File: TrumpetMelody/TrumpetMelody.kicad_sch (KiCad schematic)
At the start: 59 parts, among them J1 USB_B_Micro, J2 Conn_01x05, SW1 SW_Push, SW2 SW_SPST, SW3 SW_SPST, SW4 SW_SPST, U1 STM32F411RETx, U2 TLV62565DBVR, U3 MAX98357AETE+T, Y1 8MHz

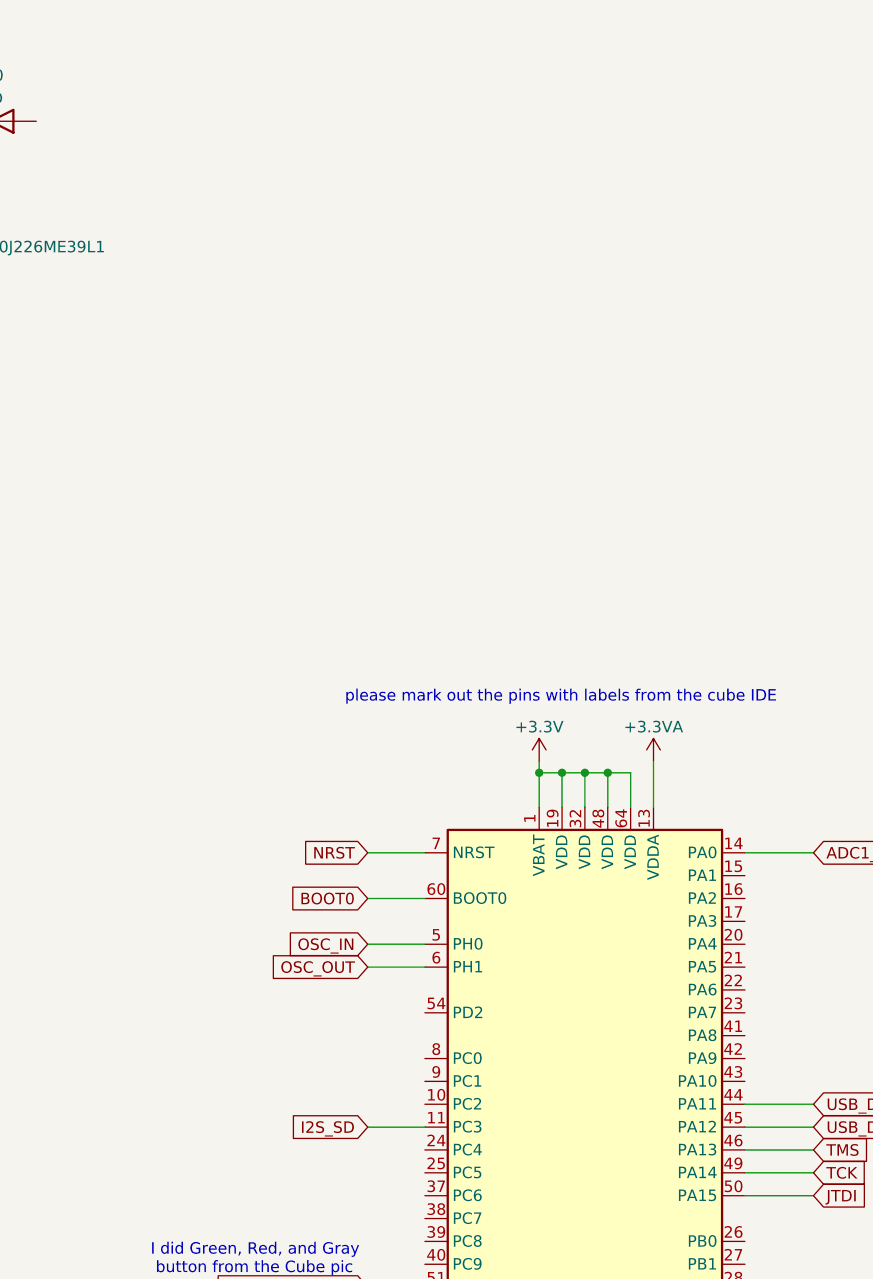
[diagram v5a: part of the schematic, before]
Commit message: Added debugging LEDs
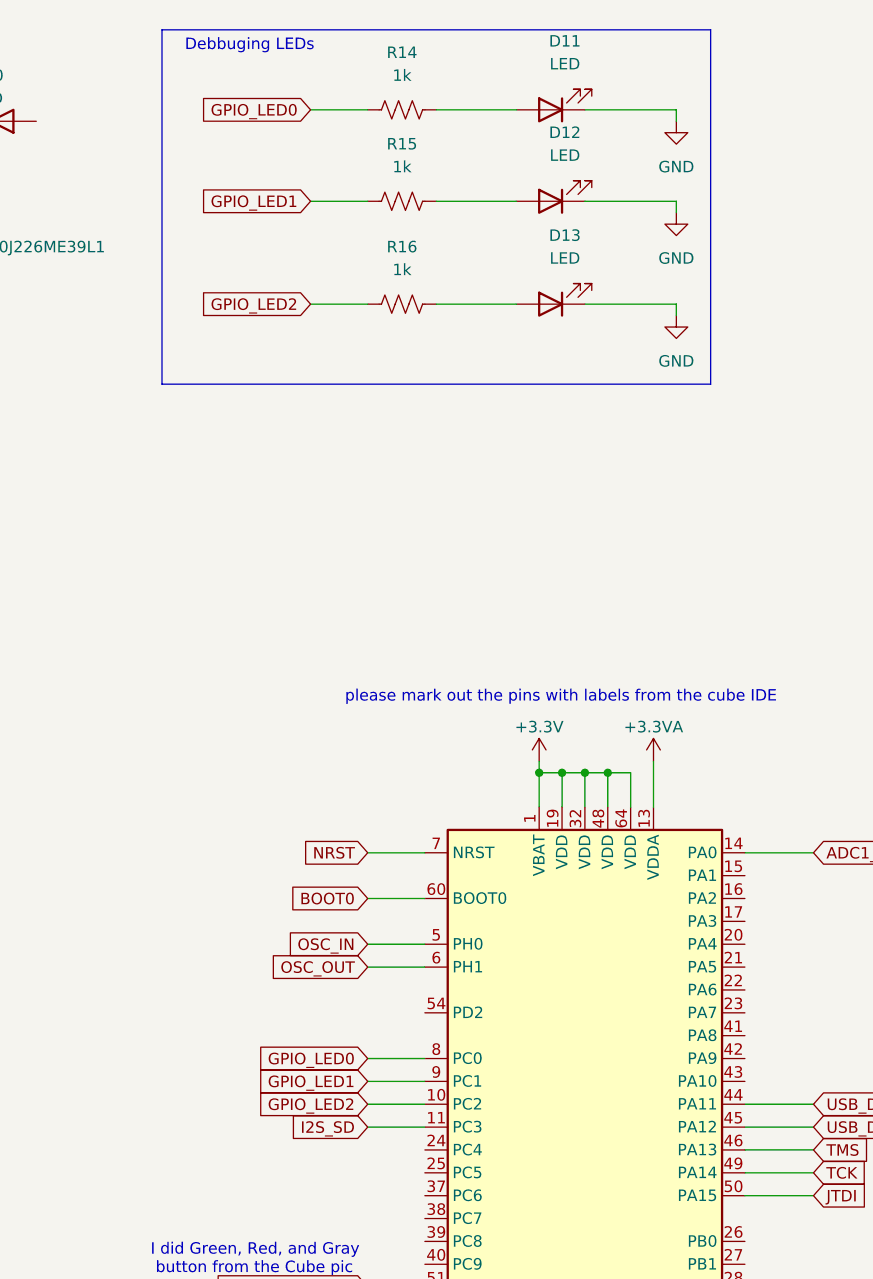
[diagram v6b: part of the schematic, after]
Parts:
- added D11, D12, D13: LED, LED_SMD:LED_0805_2012Metric_Pad1.15x1.40mm_HandSolder, symbol Device:LED
- added R14, R15, R16: 1k, Resistor_SMD:R_0805_2012Metric_Pad1.20x1.40mm_HandSolder, symbol Device:R_US
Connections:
- net GND: now also D11.1 (K), D12.1 (K), D13.1 (K)
- net GPIO_LED2: now reaches U1.10 (PC2)
- net GPIO_LED2: now also R16.1
- net GPIO_LED0: now reaches U1.8 (PC0)
- net GPIO_LED0: now also R14.1
- net GPIO_LED1: now reaches U1.9 (PC1)
- net GPIO_LED1: now also R15.1
- new net: D12.2 (A), R15.2
- new net: D13.2 (A), R16.2
- new net: D11.2 (A), R14.2
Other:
- note added: "Debbuging LEDs"

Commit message: edited more LEDs
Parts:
- added R17, R18, R19, R20: 1k, Resistor_SMD:R_0805_2012Metric_Pad1.20x1.40mm_HandSolder, symbol Device:R_US
- R10, R5, R7: value 20 -> 220
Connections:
- net +3.3V: now also R17.1
- net GND: now also D10.1 (K), D7.1 (K), D8.1 (K), D9.1 (K)
- net GPIO_BUTTON_0: now also R18.2
- net GPIO_BUTTON_1: now also R19.2
- net GPIO_BUTTON_2: now also R20.2
- net at D10.2 (A): now also R17.2
- net at D8.2 (A): now also R18.1
- net at D7.2 (A): now also R19.1
- net at D9.2 (A): now also R20.1
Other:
- note added: "Three pushbuttons with tester LEDs and ESD protection"
- note removed: "ESD protection"
- note removed: "Put Push Buttons here"
- moved on the sheet: D10, D11, D12, D13, D2, D3, D4, D7, D8, D9, R10, R14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

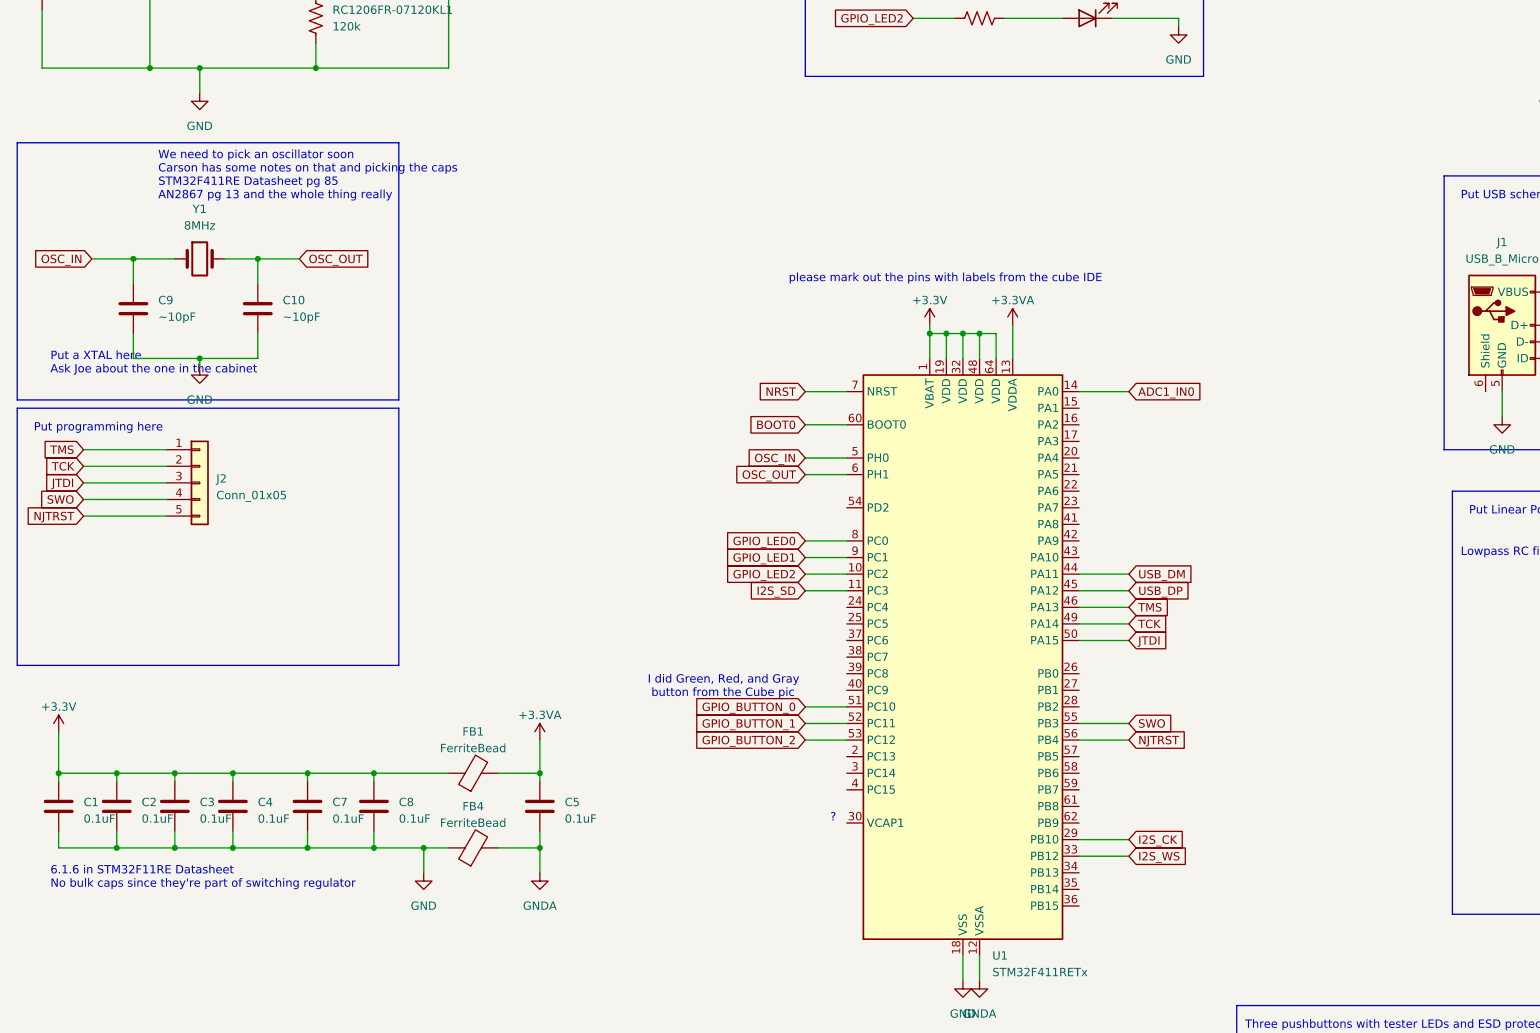
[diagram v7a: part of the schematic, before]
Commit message: Added labels to every pin
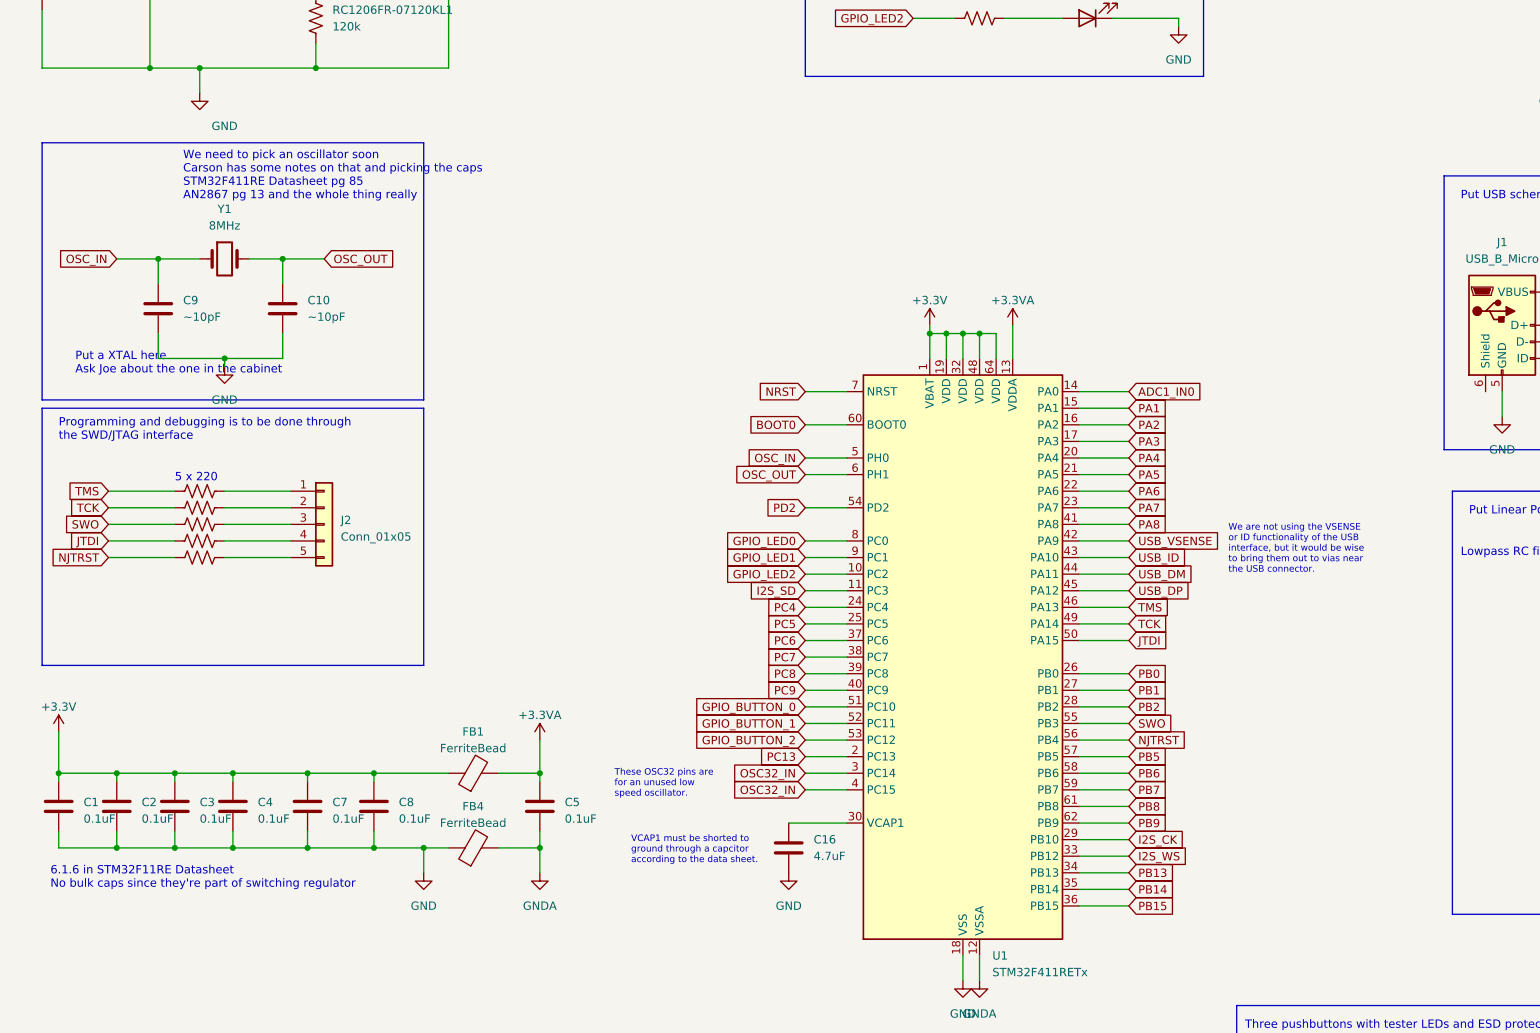
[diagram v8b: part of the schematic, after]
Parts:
- added C16: 4.7uF, Capacitor_SMD:C_0805_2012Metric_Pad1.18x1.45mm_HandSolder, symbol Device:C
- added R21, R22, R23, R24, R25: 220, symbol Device:R_US
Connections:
- net GND: now also C16.2
- net JTDI: now also R24.1; no longer J2.3 (Pin_3)
- net NJTRST: now also R25.1; no longer J2.5 (Pin_5)
- net SWO: now also R23.1; no longer J2.4 (Pin_4)
- net TCK: now also R22.1; no longer J2.2 (Pin_2)
- net TMS: now also R21.1; no longer J2.1 (Pin_1)
- net PA1: now reaches U1.15 (PA1)
- net PA2: now reaches U1.16 (PA2)
- net PA3: now reaches U1.17 (PA3)
- net PC13: now reaches U1.2 (PC13)
- net PA4: now reaches U1.20 (PA4)
- net PA5: now reaches U1.21 (PA5)
- net PA6: now reaches U1.22 (PA6)
- net PA7: now reaches U1.23 (PA7)
- net PC4: now reaches U1.24 (PC4)
- net PC5: now reaches U1.25 (PC5)
- net PB0: now reaches U1.26 (PB0)
- net PB1: now reaches U1.27 (PB1)
- net PB2: now reaches U1.28 (PB2)
- net OSC32_IN: now reaches U1.3 (PC14)
- net OSC32_IN: now also U1.4 (PC15)
- net at U1.30 (VCAP1): now also C16.1
- net PB13: now reaches U1.34 (PB13)
- net PB14: now reaches U1.35 (PB14)
- net PB15: now reaches U1.36 (PB15)
- net PC6: now reaches U1.37 (PC6)
- net PC7: now reaches U1.38 (PC7)
- net PC8: now reaches U1.39 (PC8)
- net PC9: now reaches U1.40 (PC9)
- net PA8: now reaches U1.41 (PA8)
- net USB_VSENSE: now reaches U1.42 (PA9)
- net USB_ID: now reaches U1.43 (PA10)
- net PD2: now reaches U1.54 (PD2)
- net PB5: now reaches U1.57 (PB5)
- net PB6: now reaches U1.58 (PB6)
- net PB7: now reaches U1.59 (PB7)
- net PB8: now reaches U1.61 (PB8)
- net PB9: now reaches U1.62 (PB9)
- new net: J2.4 (Pin_4), R24.2
- new net: J2.5 (Pin_5), R25.2
- new net: J2.1 (Pin_1), R21.2
- new net: J2.2 (Pin_2), R22.2
- new net: J2.3 (Pin_3), R23.2
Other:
- note added: "5 x 220"
- note added: "Programming and debugging is to be done through the SWD/JTAG interface"
- note added: "These OSC32 pins are for an unused low speed oscillator."
- note added: "VCAP1 must be shorted to ground through a capcitor according to the data sheet."
- note added: "We are not using the VSENSE or ID functionality of the USB interface, but it would be wise to bring them out to vias near the USB connector."
- note removed: "?"
- note removed: "I did Green, Red, and Gray button from the Cube pic"
- note removed: "Put programming here"
- note removed: "please mark out the pins with labels from the cube IDE"
- moved on the sheet: C10, C9, J2, Y1
